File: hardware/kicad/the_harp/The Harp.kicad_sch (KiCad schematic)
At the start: 0 parts

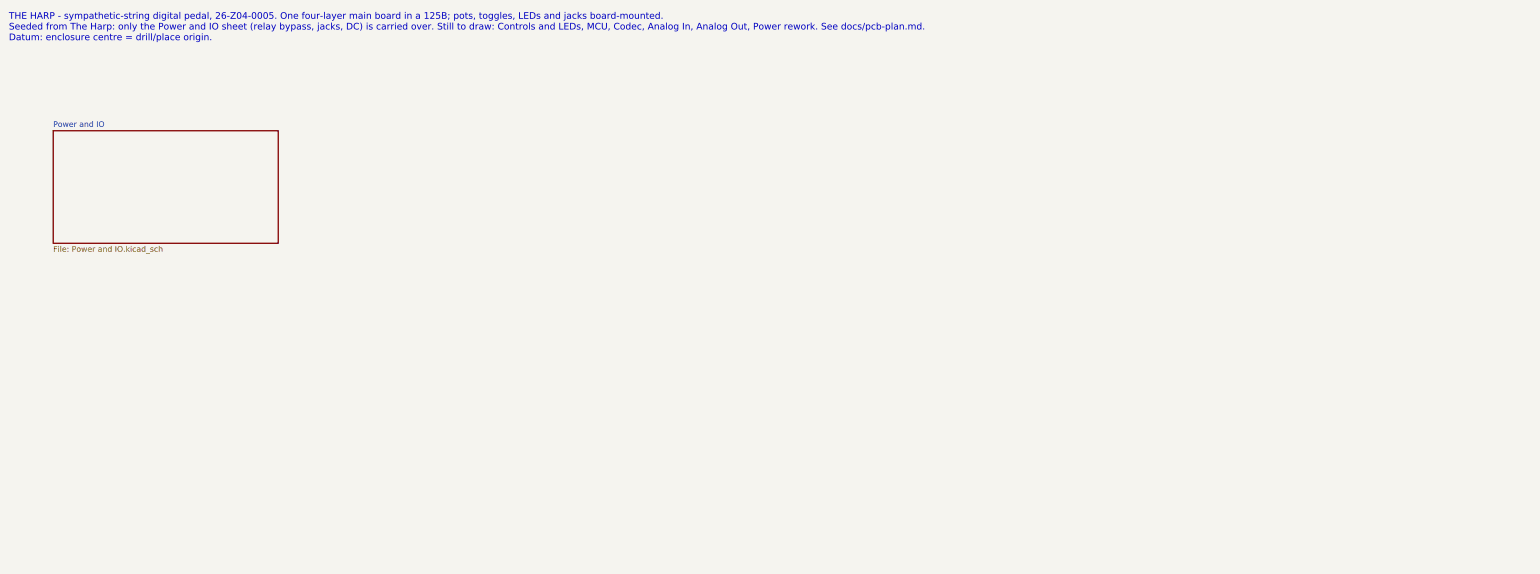
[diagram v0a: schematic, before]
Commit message: Draw the first schematic: Timekeeper circuits on the Relic grid
Seven sheets generated by scripts/harp_schematic from a circuit spec and
net-traced against it (195 parts, 48 global nets, no shorts or single-pin
nets): Controls and LEDs, MCU (STM32H750VBT6 LQFP-100, W25Q128 on QUADSPI
bank 2), Power (TPS54202 + NCP718, as the Timekeeper), Jacks and Bypass
(four jacks, Relic relay bypass, LED drivers, footswitches, expression
buffer), Codec (AK4621EF, OPA2348 VCOM buffers), ADC Driver (THS4522) and
Analog In and Out (OPA1656 buffer, OPA1688 difference amplifiers).

Replaces the Relic Power and IO sheet; removes its regulator footprints
from the board and detaches the remaining footprints for relinking by
reference. Docs: shared Alchemist/Relic/Harp face standard and the toggle
conflict it exposes, pin map, differences from the Timekeeper.

Co-Authored-By: Claude Opus 5.5 <noreply@anthropic.com>
Claude-Session: https://claude.ai/code/session_01ToUUHuo6mg178NkLtQkDLg
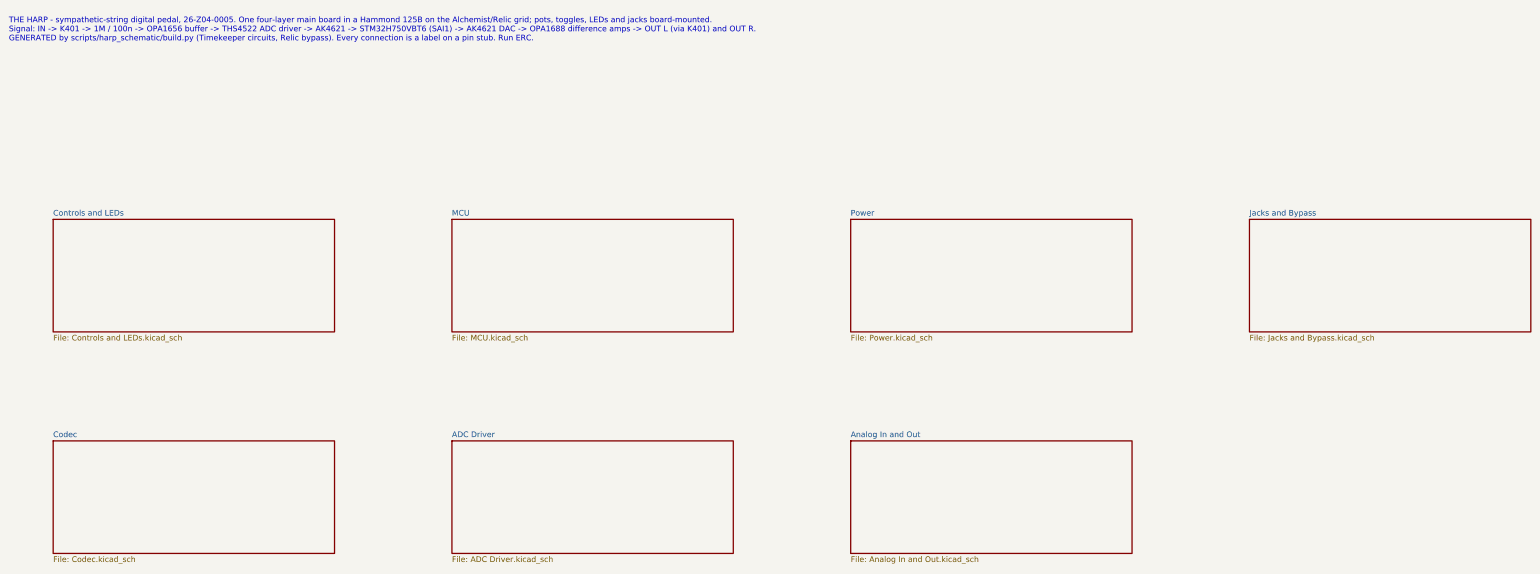
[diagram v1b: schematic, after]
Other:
- removed sheet Power and IO
- added sheet ADC Driver (ADC Driver.kicad_sch)
- added sheet Analog In and Out (Analog In and Out.kicad_sch)
- added sheet Codec (Codec.kicad_sch)
- added sheet Controls and LEDs (Controls and LEDs.kicad_sch)
- added sheet Jacks and Bypass (Jacks and Bypass.kicad_sch)
- added sheet MCU (MCU.kicad_sch)
- added sheet Power (Power.kicad_sch)
- note added: "THE HARP - sympathetic-string digital pedal, 26-Z04-0005. One four-layer main board in a Hammond 125B on the Alchemist/Relic grid; pots, toggles, LEDs and jacks board-mounted. Signal: IN -> K401 -> 1M / 100n -> OPA1656 buffer -> THS4522 ADC driver -> AK4621 -> STM32H750VBT6 (SAI1) -> AK4621 DAC -> OPA1688 difference amps -> OUT L (via K401) and OUT R. GENERATED by scripts/harp_schematic/build.py 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"
- note removed: "THE HARP - sympathetic-string digital pedal, 26-Z04-0005. One four-layer main board in a 125B; pots, toggles, LEDs and jacks board-mounted. Seeded from The Harp: only the Power and IO sheet (relay bypass, jacks, DC) is carried over. Still to draw: Controls and LEDs, MCU, Codec, Analog In, Analog Out, Power rework. See docs/pcb-plan.md. Datum: enclosure centre = drill/place origin."

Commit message: Drop the THS4522: drive the ADC from the input OPA1656
The spare half of the input OPA1656 becomes a unity inverter about VCOM_A,
so U701A drives AINL+ and U701B drives AINL- through the THS4522 stage's
own output filter (40.2R per leg, 2.7n across, 100p to GND). Removes the
ADC Driver sheet (THS4522 and 16 passives) and, with it, the Timekeeper's
floating IN_N defect. 6 sheets, 183 parts, net check clean.

Co-Authored-By: Claude Opus 5.5 <noreply@anthropic.com>
Claude-Session: https://claude.ai/code/session_01ToUUHuo6mg178NkLtQkDLg
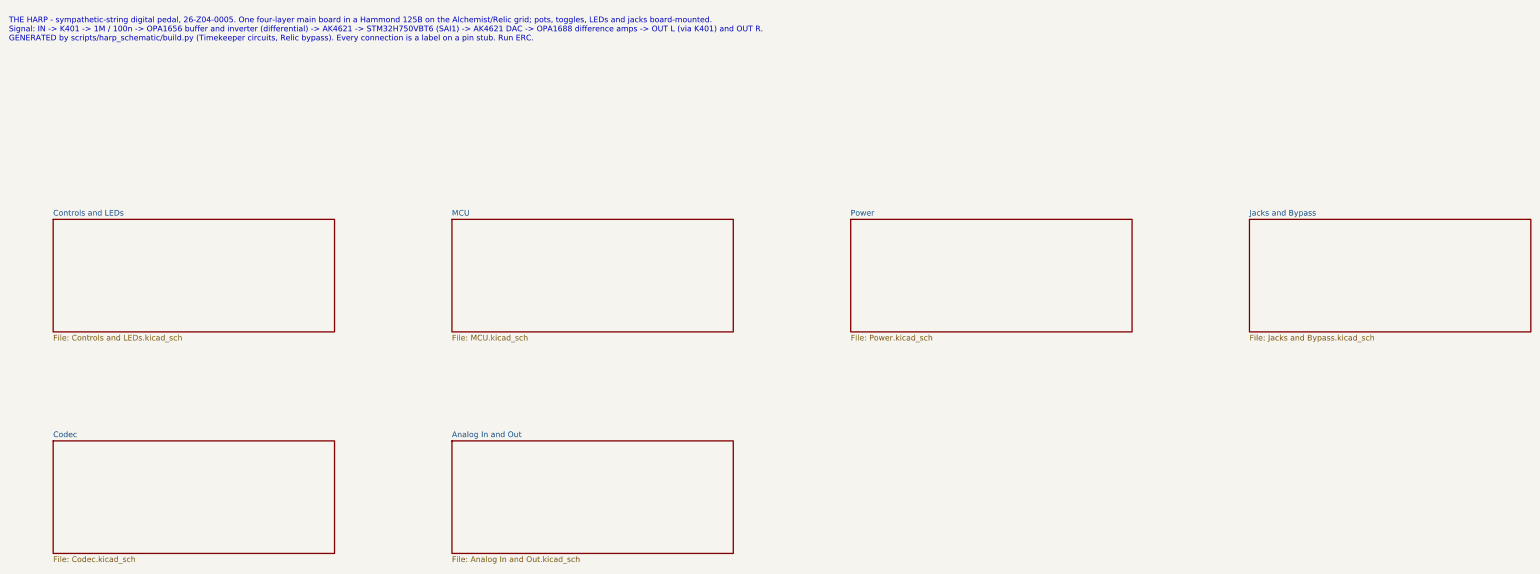
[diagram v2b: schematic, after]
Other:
- removed sheet ADC Driver
- note added: "THE HARP - sympathetic-string digital pedal, 26-Z04-0005. One four-layer main board in a Hammond 125B on the Alchemist/Relic grid; pots, toggles, LEDs and jacks board-mounted. Signal: IN -> K401 -> 1M / 100n -> OPA1656 buffer and inverter (differential) -> AK4621 -> STM32H750VBT6 (SAI1) -> AK4621 DAC -> OPA1688 difference amps -> OUT L (via K401) and OUT R. GENERATED by scripts/harp_schematic/bui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"
- note removed: "THE HARP - sympathetic-string digital pedal, 26-Z04-0005. One four-layer main board in a Hammond 125B on the Alchemist/Relic grid; pots, toggles, LEDs and jacks board-mounted. Signal: IN -> K401 -> 1M / 100n -> OPA1656 buffer -> THS4522 ADC driver -> AK4621 -> STM32H750VBT6 (SAI1) -> AK4621 DAC -> OPA1688 difference amps -> OUT L (via K401) and OUT R. GENERATED by scripts/harp_schematic/build.py 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"
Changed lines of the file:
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@@
 		(company "The Frogmouth")
 	)
-	(text "THE HARP - sympathetic-string digital pedal, 26-Z04-0005. One four-layer main board in a Hammond 125B on the Alchemist/Relic grid; pots, toggles, LEDs and jacks board-mounted.\nSignal: IN -> K401 -> 1M / 100n -> OPA1656 buffer -> THS4522 ADC driver -> AK4621 -> STM32H750VBT6 (SAI1) -> AK4621 DAC -> OPA1688 difference amps -> OUT L (via K401) and OUT R.\nGENERATED by scripts/harp_schematic/build.py (Timekeeper circuits, Relic bypass). Every connection is a label on a pin stub. Run ERC."
+	(text "THE HARP - sympathetic-string digital pedal, 26-Z04-0005. One four-layer main board in a Hammond 125B on the Alchemist/Relic grid; pots, toggles, LEDs and jacks board-mounted.\nSignal: IN -> K401 -> 1M / 100n -> OPA1656 buffer and inverter (differential) -> AK4621 -> STM32H750VBT6 (SAI1) -> AK4621 DAC -> OPA1688 difference amps -> OUT L (via K401) and OUT R.\nGENERATED by scripts/harp_schematic/build.py (Timekeeper circuits, Relic bypass). Every connection is a label on a pin stub. Run ERC."
 		(exclude_from_sim no)
 		(at 30 30 0)
@@
 			(color 0 0 0 0)
 		)
-		(property "Sheetname" "ADC Driver"
+		(property "Sheetname" "Analog In and Out"
 			(at 130 119.3 0)
 			(show_name no)
@@
 			)
 		)
-		(property "Sheetfile" "ADC Driver.kicad_sch"
+		(property "Sheetfile" "Analog In and Out.kicad_sch"
 			(at 130 146 0)
 			(show_name no)
@@
 				)
 			)
-		)
-	)
-	(sheet
-		(at 220 120)
-		(size 63.5 25.4)
-		(exclude_from_sim no)
-		(in_bom yes)
-		(on_board yes)
-		(dnp no)
-		(fields_autoplaced yes)
-		(stroke
-			(width 0.152)
-			(type solid)
-		)
-		(fill
-			(color 0 0 0 0)
-		)
-		(property "Sheetname" "Analog In and Out"
-			(at 220 119.3 0)
-			(show_name no)
-			(do_not_autoplace no)
-			(effects
-				(font
-					(size 1.27 1.27)
-				)
-				(justify left bottom)
-			)
-		)
-		(property "Sheetfile" "Analog In and Out.kicad_sch"
-			(at 220 146 0)
-			(show_name no)
-			(do_not_autoplace no)
-			(effects
-				(font
-					(size 1.27 1.27)
-				)
-				(justify left top)
-			)
-		)
-		(instances
-			(project "The Harp"
-				(path "/596641a7-eeca-47a8-9244-68f1910acd88"
-					(page "8")
-				)
-			)

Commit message: Restore the THS4522 ADC driver
Reverts c744d80. The THS4522 is designed for the single 5 V analog rail
(rail-to-rail output, VOCM sets the output common mode at the codec's VCOM),
which is why the Timekeeper uses it; the OPA1656 sits at the bottom of its
supply range there. The reference leg stays tied to VCOM_A, the fix from the
Timekeeper's input noise review (H1), not left floating.

Co-Authored-By: Claude Opus 5.5 <noreply@anthropic.com>
Claude-Session: https://claude.ai/code/session_01ToUUHuo6mg178NkLtQkDLg
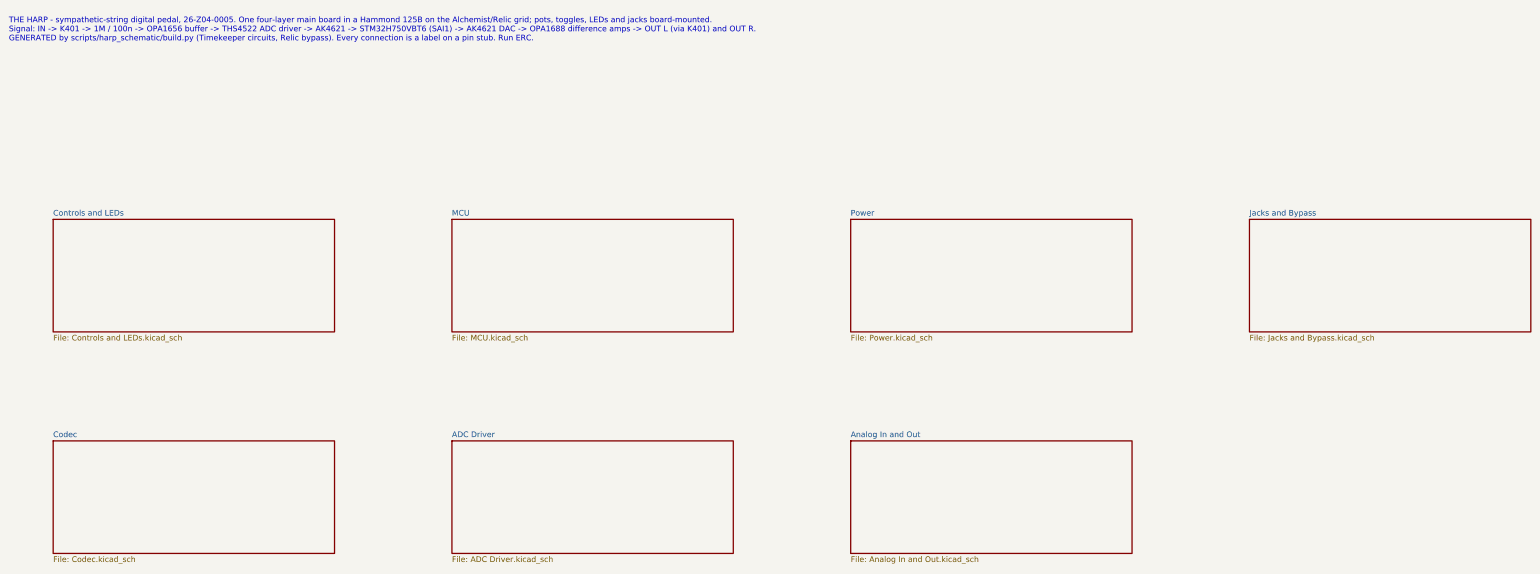
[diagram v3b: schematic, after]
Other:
- added sheet ADC Driver (ADC Driver.kicad_sch)
- note added: "THE HARP - sympathetic-string digital pedal, 26-Z04-0005. One four-layer main board in a Hammond 125B on the Alchemist/Relic grid; pots, toggles, LEDs and jacks board-mounted. Signal: IN -> K401 -> 1M / 100n -> OPA1656 buffer -> THS4522 ADC driver -> AK4621 -> STM32H750VBT6 (SAI1) -> AK4621 DAC -> OPA1688 difference amps -> OUT L (via K401) and OUT R. GENERATED by scripts/harp_schematic/build.py 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"
- note removed: "THE HARP - sympathetic-string digital pedal, 26-Z04-0005. One four-layer main board in a Hammond 125B on the Alchemist/Relic grid; pots, toggles, LEDs and jacks board-mounted. Signal: IN -> K401 -> 1M / 100n -> OPA1656 buffer and inverter (differential) -> AK4621 -> STM32H750VBT6 (SAI1) -> AK4621 DAC -> OPA1688 difference amps -> OUT L (via K401) and OUT R. GENERATED by scripts/harp_schematic/bui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"
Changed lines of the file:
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@@
 		(company "The Frogmouth")
 	)
-	(text "THE HARP - sympathetic-string digital pedal, 26-Z04-0005. One four-layer main board in a Hammond 125B on the Alchemist/Relic grid; pots, toggles, LEDs and jacks board-mounted.\nSignal: IN -> K401 -> 1M / 100n -> OPA1656 buffer and inverter (differential) -> AK4621 -> STM32H750VBT6 (SAI1) -> AK4621 DAC -> OPA1688 difference amps -> OUT L (via K401) and OUT R.\nGENERATED by scripts/harp_schematic/build.py (Timekeeper circuits, Relic bypass). Every connection is a label on a pin stub. Run ERC."
+	(text "THE HARP - sympathetic-string digital pedal, 26-Z04-0005. One four-layer main board in a Hammond 125B on the Alchemist/Relic grid; pots, toggles, LEDs and jacks board-mounted.\nSignal: IN -> K401 -> 1M / 100n -> OPA1656 buffer -> THS4522 ADC driver -> AK4621 -> STM32H750VBT6 (SAI1) -> AK4621 DAC -> OPA1688 difference amps -> OUT L (via K401) and OUT R.\nGENERATED by scripts/harp_schematic/build.py (Timekeeper circuits, Relic bypass). Every connection is a label on a pin stub. Run ERC."
 		(exclude_from_sim no)
 		(at 30 30 0)
@@
 			(color 0 0 0 0)
 		)
+		(property "Sheetname" "ADC Driver"
+			(at 130 119.3 0)
+			(show_name no)
+			(do_not_autoplace no)
+			(effects
+				(font
+					(size 1.27 1.27)
+				)
+				(justify left bottom)
+			)
+		)
+		(property "Sheetfile" "ADC Driver.kicad_sch"
+			(at 130 146 0)
+			(show_name no)
+			(do_not_autoplace no)
+			(effects
+				(font
+					(size 1.27 1.27)
+				)
+				(justify left top)
+			)
+		)
+		(instances
+			(project "The Harp"
+				(path "/596641a7-eeca-47a8-9244-68f1910acd88"
+					(page "7")
+				)
+			)
+		)
+	)
+	(sheet
+		(at 220 120)
+		(size 63.5 25.4)
+		(exclude_from_sim no)
+		(in_bom yes)
+		(on_board yes)
+		(dnp no)
+		(fields_autoplaced yes)
+		(stroke
+			(width 0.152)
+			(type solid)
+		)
+		(fill
+			(color 0 0 0 0)
+		)
 		(property "Sheetname" "Analog In and Out"
-			(at 130 119.3 0)
+			(at 220 119.3 0)
 			(show_name no)
 			(do_not_autoplace no)
@@
 		)
 		(property "Sheetfile" "Analog In and Out.kicad_sch"
-			(at 130 146 0)
-			(show_name no)
-			(do_not_autoplace no)
-			(effects
-				(font
-					(size 1.27 1.27)
-				)
-				(justify left top)
-			)
-		)
-		(instances
-			(project "The Harp"
-				(path "/596641a7-eeca-47a8-9244-68f1910acd88"
-					(page "7")
-				)
-			)
+			(at 220 146 0)
+			(show_name no)
+			(do_not_autoplace no)
+			(effects
+				(font
+					(size 1.27 1.27)
+				)
+				(justify left top)
+			)
+		)
+		(instances
+			(project "The Harp"
+				(path "/596641a7-eeca-47a8-9244-68f1910acd88"
+					(page "8")
+				)
+			)
